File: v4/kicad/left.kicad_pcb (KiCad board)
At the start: 2 copper layers, 158 x 119 mm, 68 parts

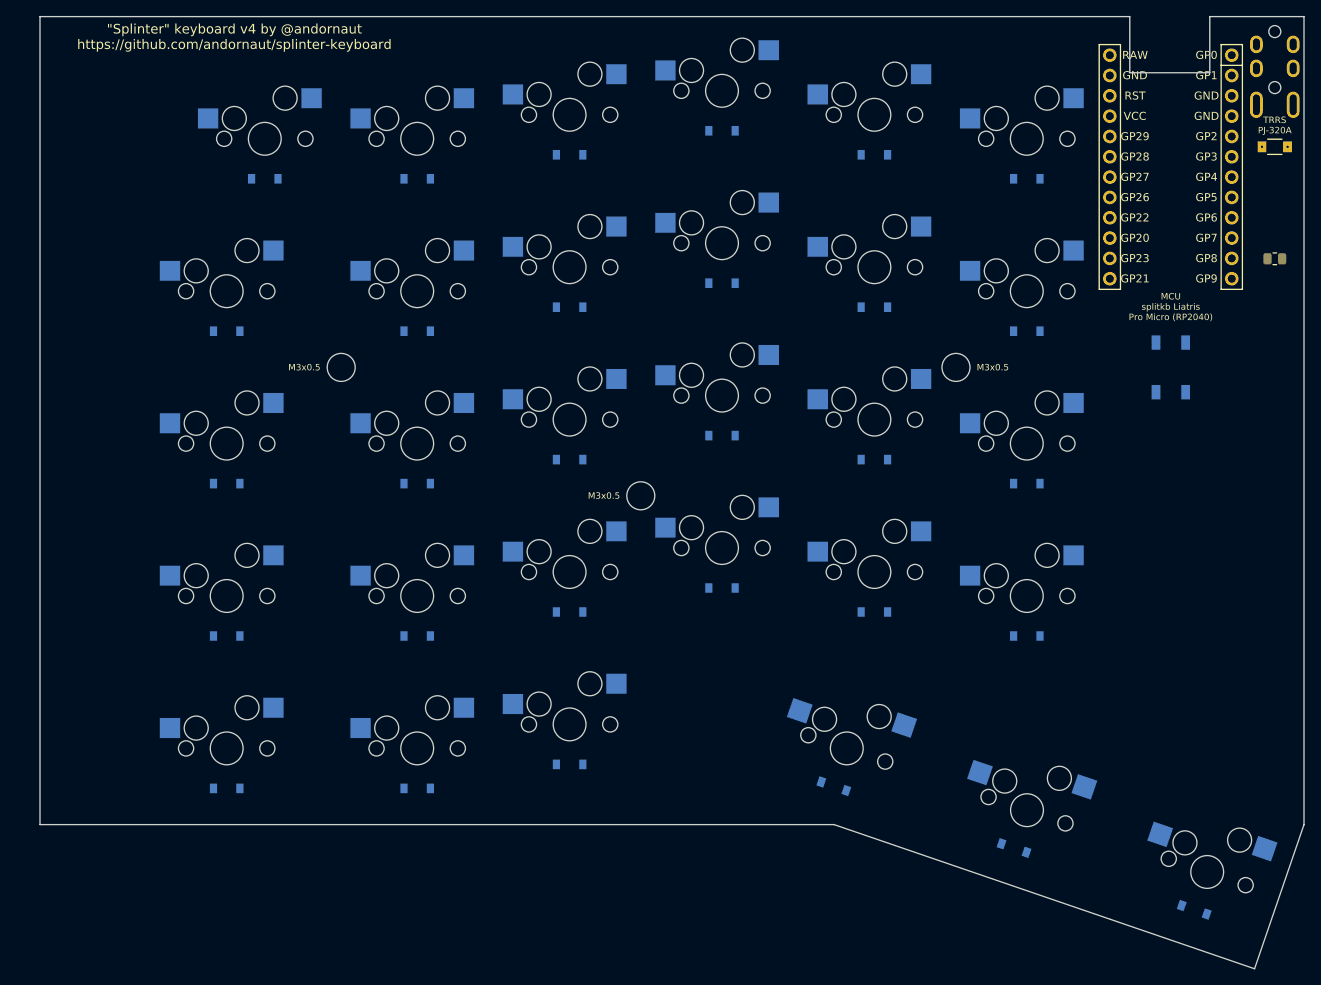
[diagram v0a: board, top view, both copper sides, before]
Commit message: v4: SMD footprints with both-side routing vias; mute pcbnew noise
Footprints:
- Add r_0805 (single-side 0805 SMD) and convert sod-123fl from reversible
  THT to single-side SMD; both gain an opt-in include_traces_vias helper
  (via just outside each pad) plus a via_in_pad option (via in the pad,
  needs filled-and-capped vias for reflow, off by default).
- config.yaml: data_resistor switched infused-kim/smd_0805 -> r_0805,
  data_tvs + data_resistor get include_traces_vias for both-side routing,
  and the matrix diode gets reversible + include_traces_vias so its net
  routes on either layer (single-side assembly unchanged).

Tooling:
- lib.sh mute_pcbnew_noise helper drops KiCad's harmless PROPERTY_ENUM
  wxASSERT from stderr; applied in build/copy scripts, and autoroute.py
  silences the same noise around its in-process pcbnew import.
- gen-jlcpcb-bom-cpl.py groups Do-Not-Place footprints by package and
  reports them so an unintended DNP is visible.

Docs: refresh README and v4/README; register r_0805 in the Dockerfile.
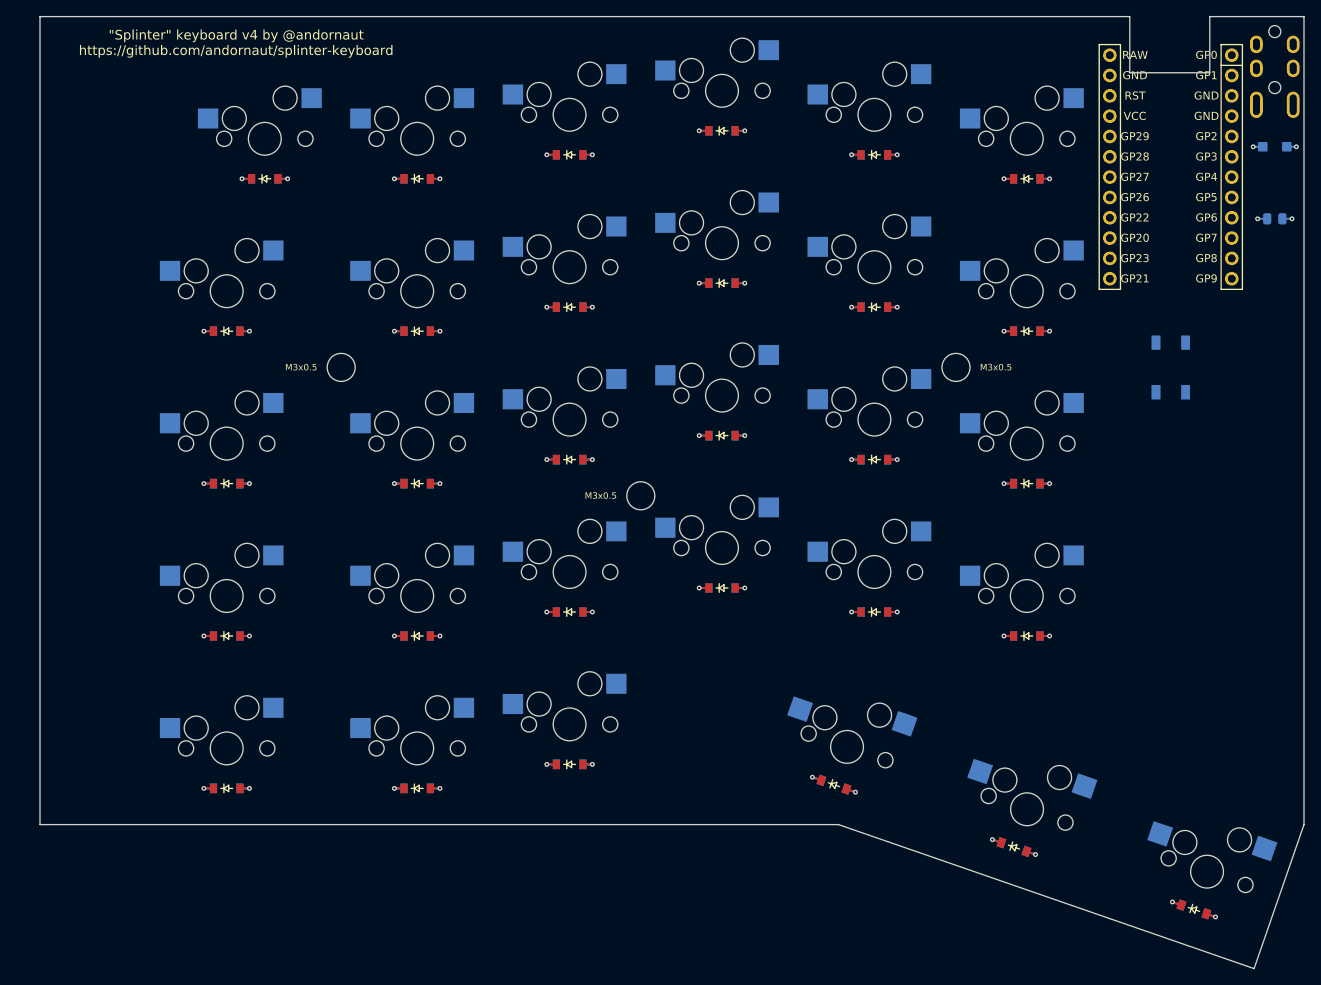
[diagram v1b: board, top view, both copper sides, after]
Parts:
- D1, D10, D11, D12, D13, D14, D15, D16, D17, D18, D19, D2, D20, D21, D22, D23, D24, D25, D26, D27, D28, D29, D3, D30, D4, D5, D6, D7, D8, D9: moved to F.Cu
- D31: footprint splinter:D_SOD-123FL_HandSolder -> splinter:D_SOD-123FL; moved to B.Cu
- R1: value (none) -> 100R; footprint smd_805 -> splinter:R_0805; moved to B.Cu
- moved R1 5.00 mm to (285.2, 113.8)
- moved D28 0.19 mm to (230.1, 184.5), turned to -19.1117 degrees
- moved S28 0.19 mm to (231.8, 179.8), turned to -19.1117 degrees
- moved D29 0.12 mm to (252.6, 192.3), turned to -19.1117 degrees
- moved S29 0.11 mm to (254.3, 187.6), turned to -19.1117 degrees
- moved D30 0.06 mm to (275.1, 200.1), turned to -19.1117 degrees
- turned S30 to -19.1117 degrees
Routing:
- net P16: track 0.00 -> 14.4 mm, vias 0 -> 6
- net P15: track 0.00 -> 14.4 mm, vias 0 -> 6
- net P14: track 0.00 -> 14.4 mm, vias 0 -> 6
- net P5: track 0.00 -> 14.4 mm, vias 0 -> 6
- net P10: track 0.00 -> 14.4 mm, vias 0 -> 6
- net zero_upper: track 0.00 -> 2.40 mm, vias 0 -> 1
- net zero_mod: track 0.00 -> 2.40 mm, vias 0 -> 1
- net zero_lower: track 0.00 -> 2.40 mm, vias 0 -> 1
- net zero_home: track 0.00 -> 2.40 mm, vias 0 -> 1
- net one_upper: track 0.00 -> 2.40 mm, vias 0 -> 1
- net one_num: track 0.00 -> 2.40 mm, vias 0 -> 1
- net one_mod: track 0.00 -> 2.40 mm, vias 0 -> 1
- net one_lower: track 0.00 -> 2.40 mm, vias 0 -> 1
- net one_home: track 0.00 -> 2.40 mm, vias 0 -> 1
- net four_upper: track 0.00 -> 2.40 mm, vias 0 -> 1
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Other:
- outline, holes or cut-outs redrawn

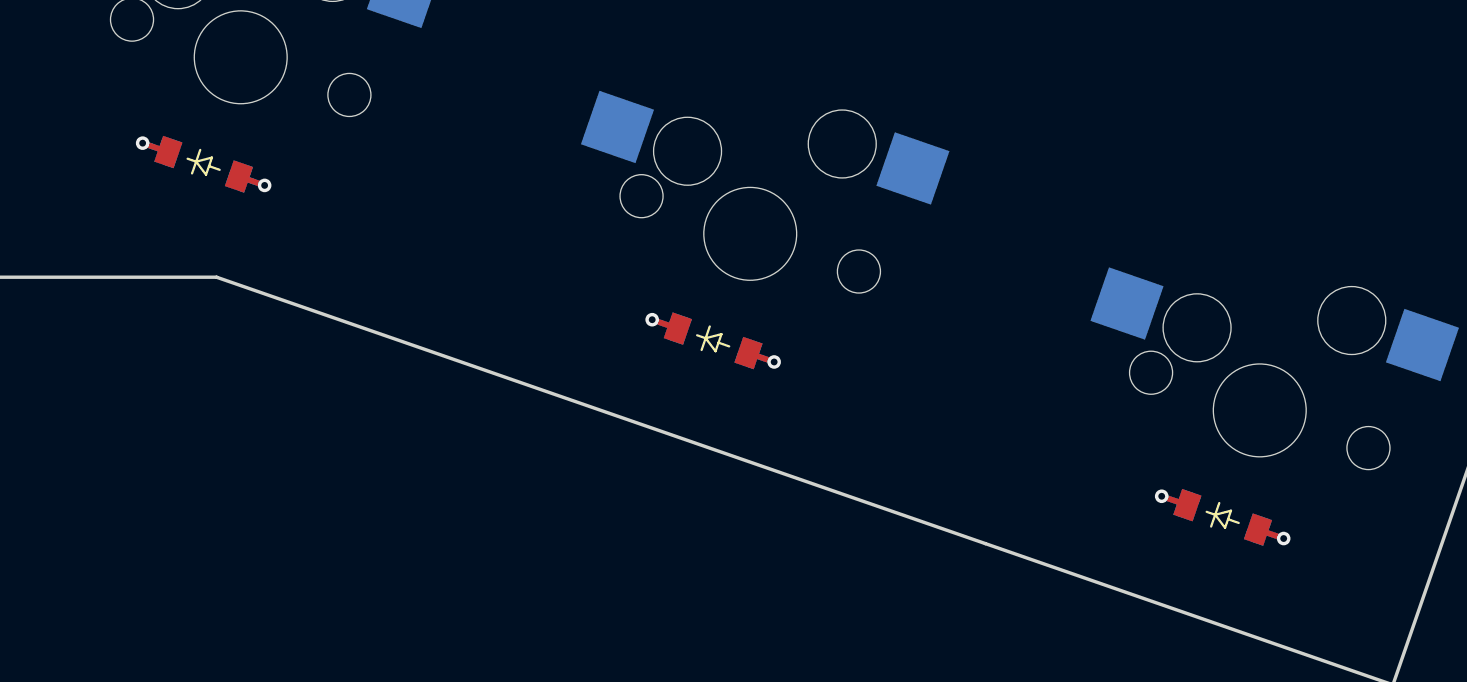
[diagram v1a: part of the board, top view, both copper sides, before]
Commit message: v4: fork SOD-123 diode footprint, counter-rotate thumb diodes; add OK success lines to scripts
Switch v4 matrix/thumb diodes from ceoloide/diode_tht_sod123 to the forked
diode_sod123 footprint (matched where: regex per key group). Thumb diodes
counter-rotate by -thumb_splay to sit horizontal, with a thumb_diode_dx nudge
to re-center under the splayed switch; both driven by single-source-of-truth
units. Re-key jlcpcb-parts.json to diode_sod123 and set rotation 180 so the
cathode band lands on pad 1 in JLC DFM.

Register diode_sod123 in the Dockerfile GUI image (sed loop over footprint
stems). Add a uniform ok() helper in lib.sh and a trailing OK: success line to
each script wrapper. Regenerate left/right PCBs (working and routed).
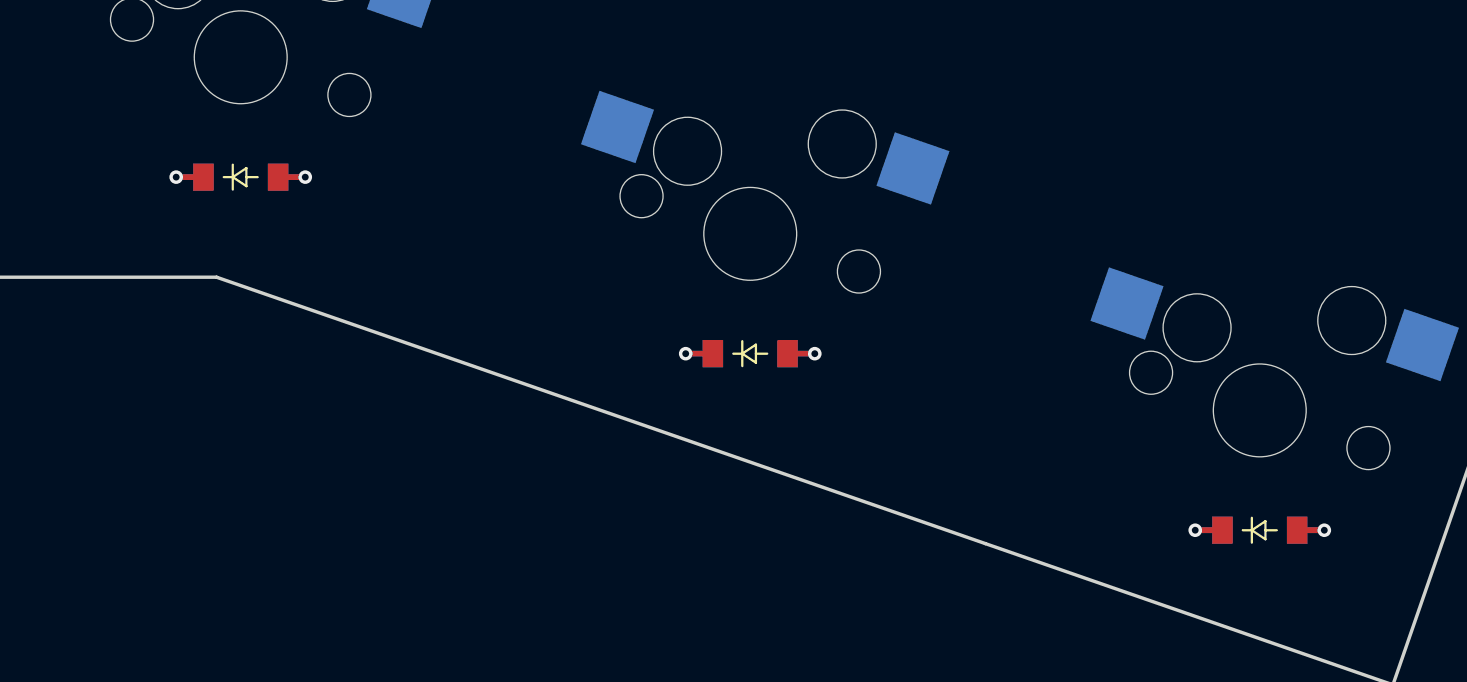
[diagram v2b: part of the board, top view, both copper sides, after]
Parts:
- D1, D10, D11, D12, D13, D14, D15, D16, D17, D18, D19, D2, D20, D21, D22, D23, D24, D25, D26, D27, D28, D29, D3, D30, D4, D5, D6, D7, D8, D9: footprint ceoloide:diode_tht_sod123 -> splinter:diode_sod123; moved to B.Cu
- moved D30 1.73 mm to (276.8, 200.7), turned to 0 degrees
- moved D29 1.73 mm to (254.3, 192.9), turned to 0 degrees
- moved D28 1.73 mm to (231.8, 185.1), turned to 0 degrees

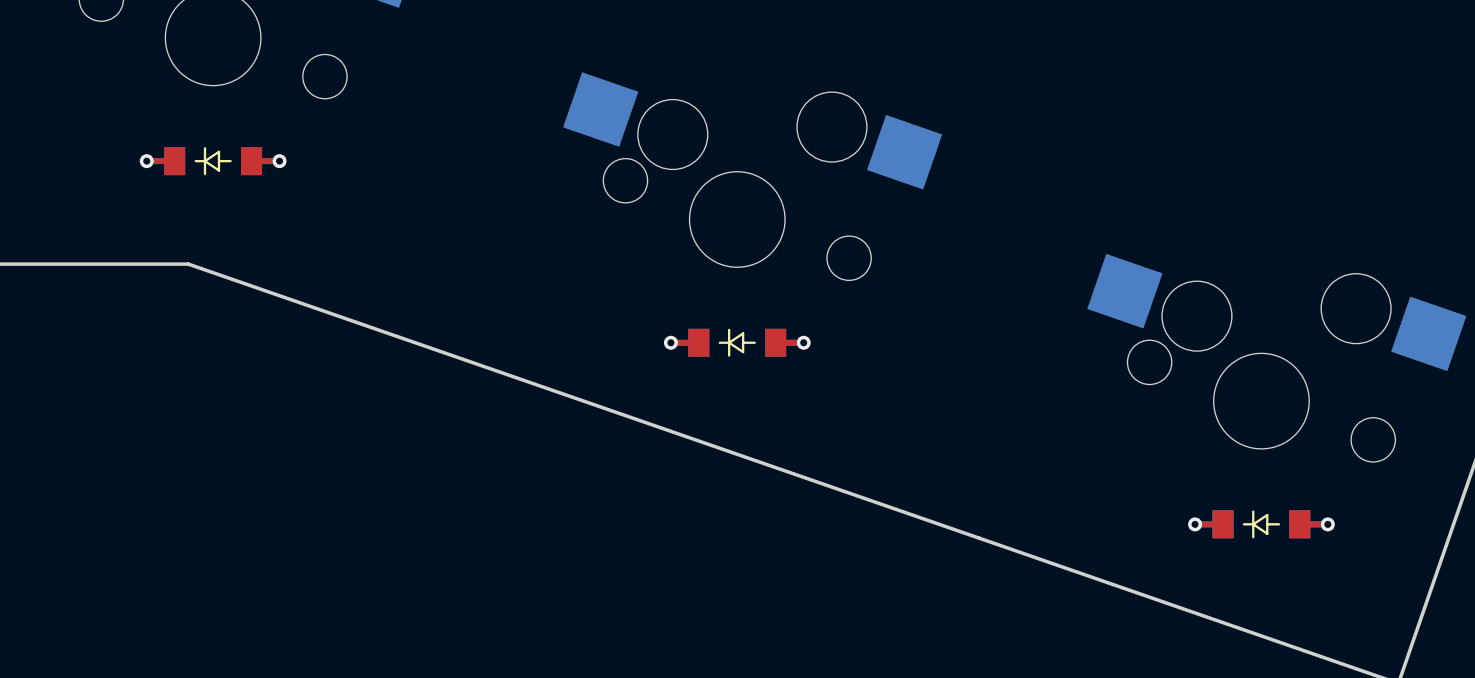
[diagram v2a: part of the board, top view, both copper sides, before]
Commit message: v4: parameterize thumb diode offset, center under switch
Add thumb_diode_dy/dx units for the horizontal thumb diodes' offset from
their splayed switches. dx re-centers laterally (the rotated dy would drift
it sideways); keep dx = dy * tan(thumb_splay) so it stays centered when dy
changes, and dx auto-flips x on the mirrored right half. Set dy to -4.7
(sits ~4.97mm below the switch, level with the matrix diodes), centered.
Regenerate both halves and the routed copies.
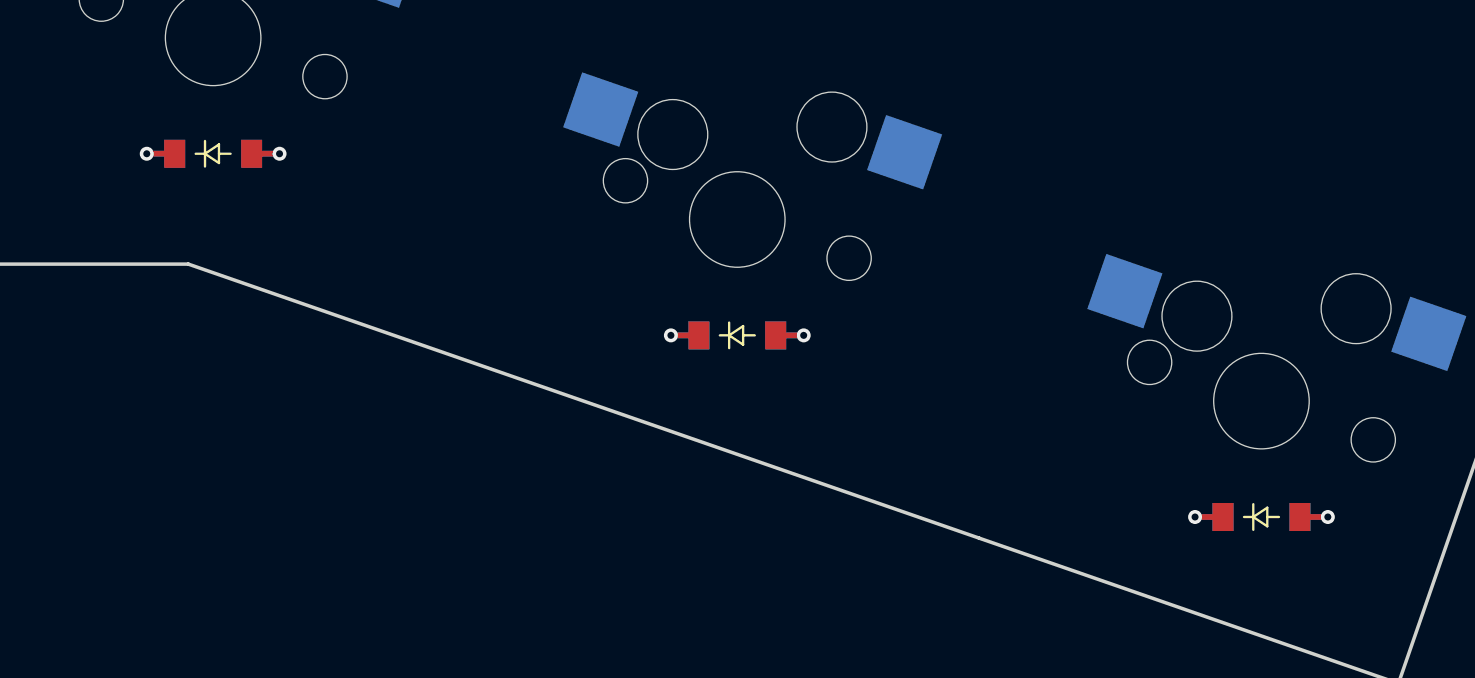
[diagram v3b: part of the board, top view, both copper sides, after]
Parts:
- moved D30 0.32 mm to (276.8, 200.4)
- moved D28 0.32 mm to (231.8, 184.8)
- moved D29 0.32 mm to (254.3, 192.6)
